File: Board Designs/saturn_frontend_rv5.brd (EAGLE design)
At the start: 95.6 x 73.6 mm, 44 parts

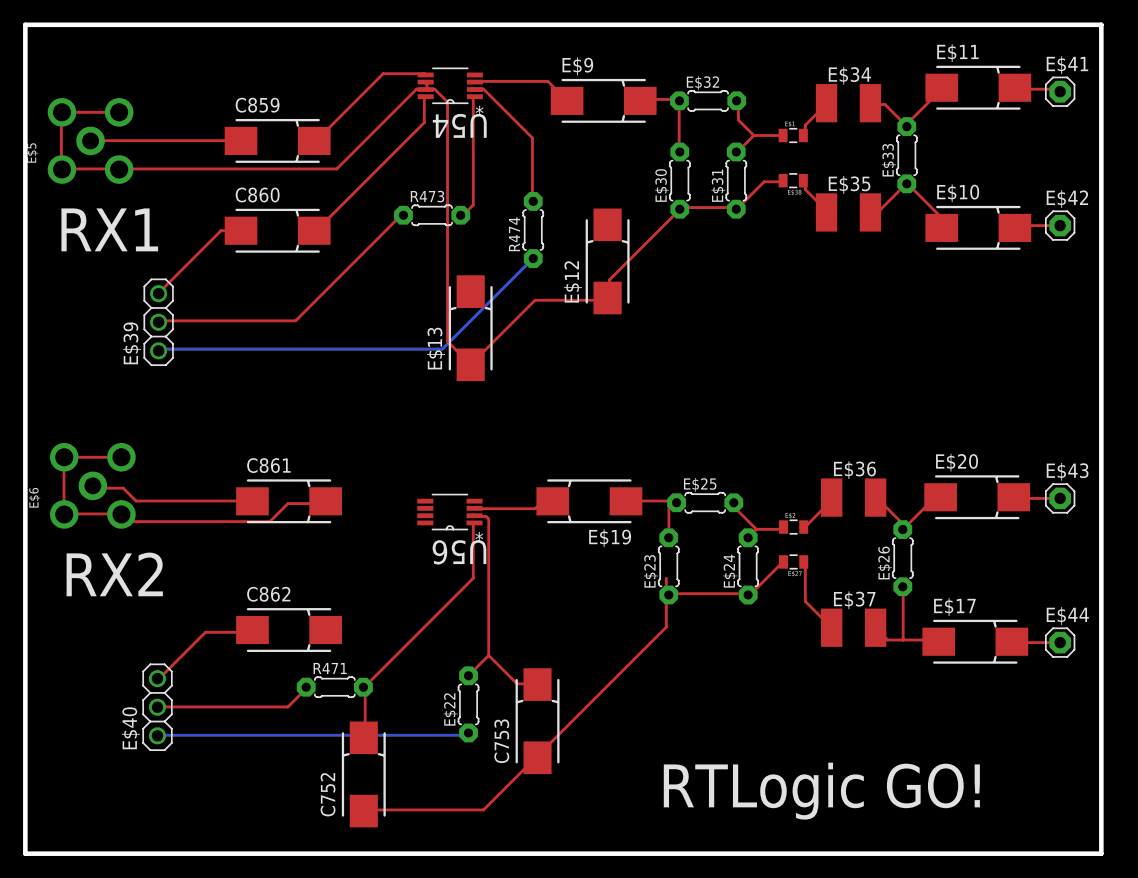
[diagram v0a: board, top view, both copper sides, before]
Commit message: Moved board designs to a seperate directory to keep SPICE/ clean
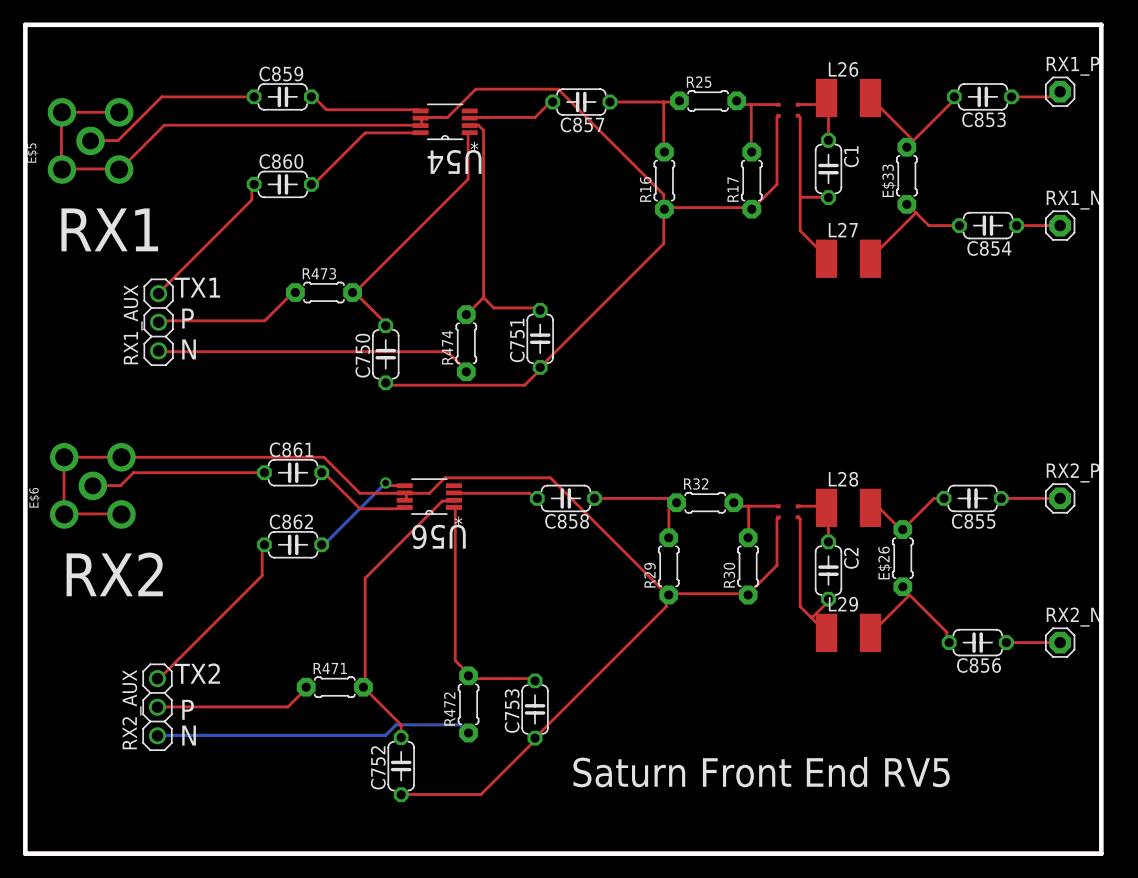
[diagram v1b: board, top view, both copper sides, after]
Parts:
- removed E$10, E$11, E$12, E$13, E$17, E$19, E$20, E$9: 100 pF, adafruit:085CS_1AR
- removed E$27, E$38: (no value), 0805:0805
- removed E$30, E$31: 221 Ohm, adafruit:0204/5
- removed E$34, E$35, E$36, E$37: 1.0 nH, eagle-ltspice:L1812
- added C1, C2: 400 fF, adafruit:C050-024X044
- added C750, C751, C853, C854, C855, C856, C857, C858: 100 pF, adafruit:C050-024X044
- added L26, L27, L28, L29: 1.0 nH, eagle-ltspice:L1812
- added R16, R17: 221 Ohm, adafruit:0204/5
- C752, C753, C859, C860, C861: device adafruit:085CS_1AR -> adafruit:C050-024X044
- C862: value 100 pF -> (none); device adafruit:085CS_1AR -> adafruit:C050-024X044
- E$1, E$2: device 0805:0805 -> cody_custom_library:BALUN_LOGICALS
- moved R473 11.8 mm to (36.1, 61.7)
- moved R474 11.7 mm to (48.8, 57.2)
- moved C862 7.58 mm to (33.4, 39.3)
- moved C860 4.14 mm to (32.5, 71.3)
- moved C859 3.94 mm to (32.5, 79.1)
- moved C752 3.40 mm to (43.0, 19.7)
- moved U54 3.23 mm to (46.9, 76.9)
- moved C861 2.56 mm to (33.4, 45.7)
- moved U56 2.29 mm to (45.5, 43.6)
- moved E$1 2.15 mm to (76.4, 77.3)
- moved E$33 1.83 mm to (87.9, 72.1)
- moved E$2 1.64 mm to (76.4, 41.6)
- moved C753 1.06 mm to (54.9, 24.7)
- renumbered E$22 to R472, E$23 to R29, E$24 to R30, E$25 to R32, E$32 to R25, E$39 to RX1_AUX, E$40 to RX2_AUX, E$41 to RX1_P, E$42 to RX1_N, E$43 to RX2_P, E$44 to RX2_N
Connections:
- removed net J11: E$12.-, E$13.-, E$30.1, E$31.1, E$38.2, E$5.GND1, E$5.GND2, E$5.GND3, E$5.GND4, U54.6, U54.7
- removed net J12: C752.-, C753.-, E$27.2, R29.1, R30.1
- removed net S$11: E$10.+, RX1_N.1
- removed net S$17: E$20.+, RX2_P.1
- removed net S$21: E$17.+, RX2_N.1
- removed net S$22: R473.2, U54.1
- removed net S$26: E$30.2, E$9.+, R25.1
- new net S$38: C859.1, E$5.ANTENNA
- new net S$46: C752.1, C753.1, E$2.2, E$6.GND1, E$6.GND2, E$6.GND3, E$6.GND4, R29.1, R30.1, U56.6, U56.7
- new net S$47: C856.1, RX2_N.1
- new net S$49: R472.1, RX2_AUX.1
- net S$1: now also E$2.1, R30.2, R32.2; no longer E$11.+, RX1_P.1
- net S$10: now also C857.1, R16.2, R25.1; no longer E$2.1, R30.2, R32.2
- net S$12: now also E$1.1, R17.2, R25.2; no longer E$11.-, E$33.2, E$34.2
- net S$14: now also C1.1, E$1.4, L26.1; no longer E$2.2, E$36.1
- net S$16: now also C1.2, E$1.3, L27.1; no longer C859.+, U54.5
- net S$18: now also C853.2, E$33.2, L26.2; no longer C860.+, U54.8
- net S$19: now also C854.2, E$33.1, L27.2; no longer E$19.+
- net S$2: now also C2.1, E$2.4, L28.1; no longer E$13.+
- net S$23: now also C853.1, RX1_P.1; no longer R474.2, U54.2
- net S$24: now also C854.1, RX1_N.1; no longer C861.+, E$6.GND1, E$6.GND2, E$6.GND3, E$6.GND4, U56.6, U56.7, U56.8
- net S$25: now also R473.1, RX1_AUX.2; no longer R474.1, RX1_AUX.1
- net S$27: now also C750.2, R473.2, U54.1; no longer E$1.1, E$31.2, R25.2
- net S$28: now also C751.2, R474.2, U54.2; no longer E$1.2, E$34.1
- net S$29: now also R474.1, RX1_AUX.1; no longer E$35.1, E$38.1
- net S$3: now also C858.1, R29.2, R32.1; no longer E$12.+
- net S$32: now also R471.1, RX2_AUX.2; no longer C862.-, RX2_AUX.3
- net S$33: now also C752.2, R471.2, U56.2; no longer R471.1, RX2_AUX.2
- net S$34: now also C753.2, R472.2, U56.1; no longer R472.1, RX2_AUX.1
- net S$35: now also C861.1, E$6.ANTENNA; no longer C862.+, U56.5
- net S$36: now also C862.1, RX2_AUX.3; no longer C861.-, E$6.ANTENNA
- net S$37: now also C860.1, RX1_AUX.3; no longer E$9.-, U54.3
- net S$39: now also C859.2, U54.5; no longer U56.3
- net S$40: now also C860.2, U54.8; no longer C752.+, R471.2, U56.1
- net S$41: now also C862.2, U56.5; no longer C753.+, R472.2, U56.2
- net S$42: now also C861.2, U56.8; no longer E$19.-, R29.2, R32.1
- net S$43: now also C858.2, U56.3; no longer E$27.1, E$37.1
- net S$44: now also C857.2, U54.3; no longer E$20.-, E$26.2, E$36.2
- net S$45: now also C750.1, C751.1, E$1.2, E$5.GND1, E$5.GND2, E$5.GND3, E$5.GND4, R16.1, R17.1, U54.6, U54.7; no longer E$17.-, E$26.1, E$37.2
- net S$5: now also C855.2, E$26.2, L28.2; no longer C859.-, E$5.ANTENNA
- net S$6: now also C855.1, RX2_P.1; no longer E$10.-, E$33.1, E$35.2
- net S$7: now also C856.2, E$26.1, L29.2; no longer C860.-, RX1_AUX.3
- net S$8: now also C2.2, E$2.3, L29.1; no longer R473.1, RX1_AUX.2
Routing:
- net S$46: track 0.00 -> 117.7 mm
- net S$45: track 10.8 -> 122.8 mm
- net J11: track 108.5 -> 0.00 mm
- net S$48: track 0.00 -> 95.6 mm
- net J12: track 50.0 -> 0.00 mm
- net S$24: track 34.5 -> 3.86 mm
- net S$49: track 0.00 -> 28.3 mm
- net S$29: track 3.68 -> 28.2 mm
- net S$25: track 36.7 -> 13.3 mm
- net S$28: track 3.81 -> 24.0 mm
- net S$38: track 0.00 -> 16.1 mm
- net S$35: track 0.08 -> 15.7 mm
- net S$27: track 8.47 -> 22.8 mm
- net S$33: track 14.0 -> 26.4 mm
- net S$8: track 25.7 -> 13.7 mm
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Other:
- board text added: "N"
- board text added: "P"
- board text added: "Saturn Front End RV5"
- board text added: "TX1"
- board text added: "TX2"
- board text removed: "RTLogic GO!"
